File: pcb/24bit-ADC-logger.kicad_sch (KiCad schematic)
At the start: 21 parts, among them U1 REF5050AD, U2 ADS1232IPW, U3 TL071, U4 MAX15062A, U5 LP38693MP-5.0, U6 PicoW

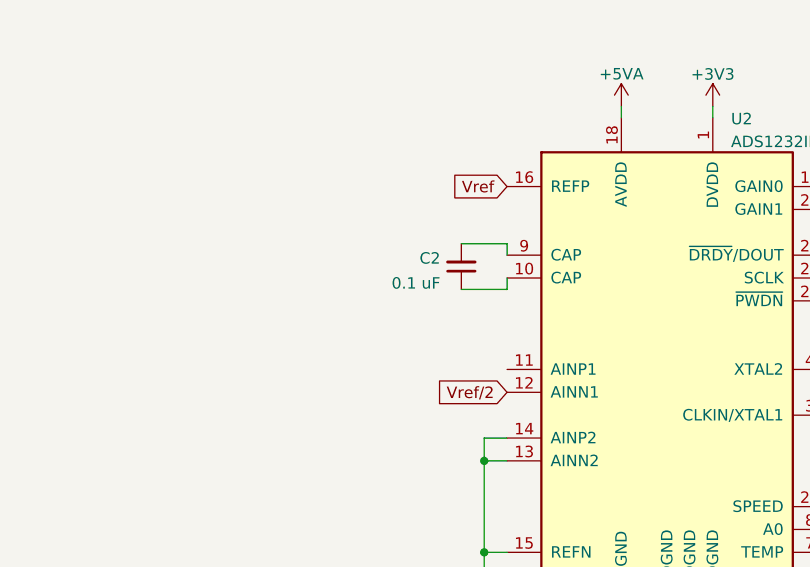
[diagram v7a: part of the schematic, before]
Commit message: Revert "test: set capacitor value to trigger CI review diff"
This reverts commit 620bb8e880ffa57cb9d26c4f289deb38077c155b.
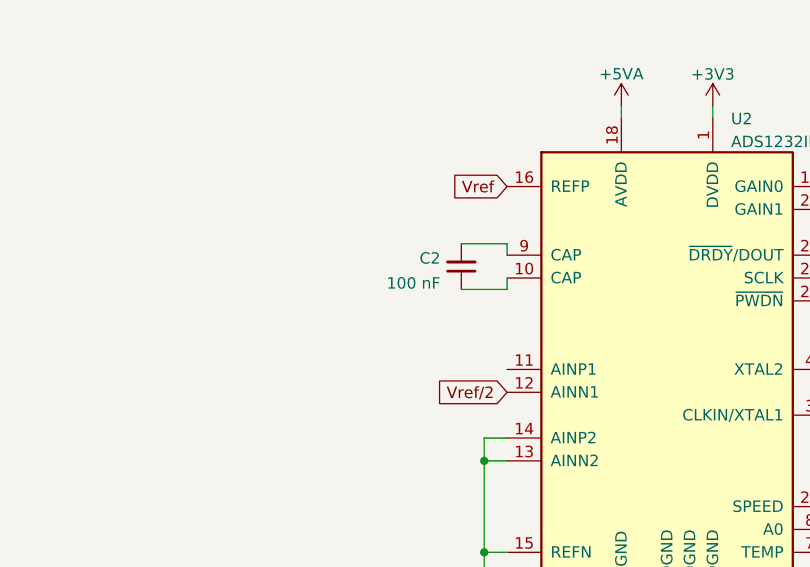
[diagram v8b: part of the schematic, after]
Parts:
- C2: value 0.1 uF -> 100 nF
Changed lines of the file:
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@@
       (effects (font (size 1.27 1.27)) (justify right))
     )
-    (property "Value" "0.1 uF" (id 1) (at 89.1159 69.1702 0)
+    (property "Value" "100 nF" (id 1) (at 89.1159 69.1702 0)
       (effects (font (size 1.27 1.27)) (justify right))
     )
@@
     )
     (path "/0fafedb4-75f0-46bd-ad25-e71605789522"
-      (reference "C2") (unit 1) (value "0.1 uF") (footprint "")
+      (reference "C2") (unit 1) (value "100 nF") (footprint "")
     )
     (path "/c2d5842f-85a0-468a-8cc5-d2ab1d5f7796"
